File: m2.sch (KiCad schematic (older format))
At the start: 16 parts, among them M2 M2_2280, U12 MDT580M01001

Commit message: Cleanup
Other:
- note removed: "Work in progress."
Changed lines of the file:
@@
 $Descr A4 11693 8268
 encoding utf-8
-Sheet 8 13
+Sheet 8 12
 Title ""
 Date ""
@@
 	1    0    0    -1
 $EndComp
-Text Notes 2725 1200 0    50   ~ 0
-Work in progress.
 Text Notes 2669 49363 0    60   ~ 0
 Text

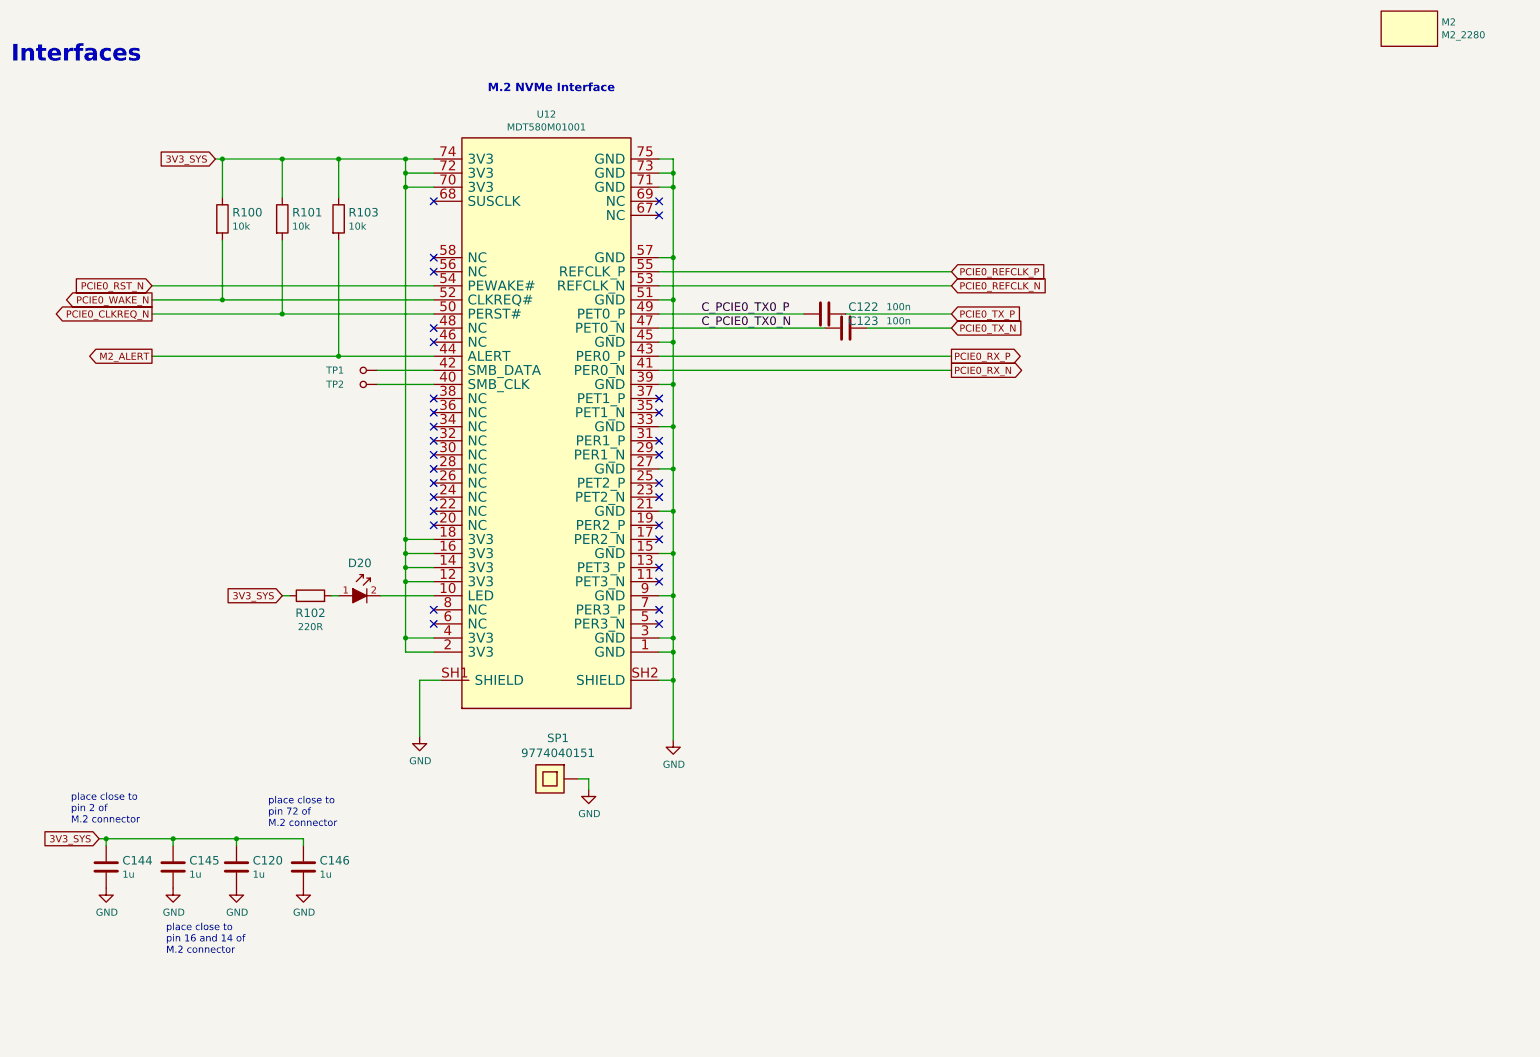
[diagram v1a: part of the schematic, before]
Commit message: Reorganize schematics, add descriptions in top left corner
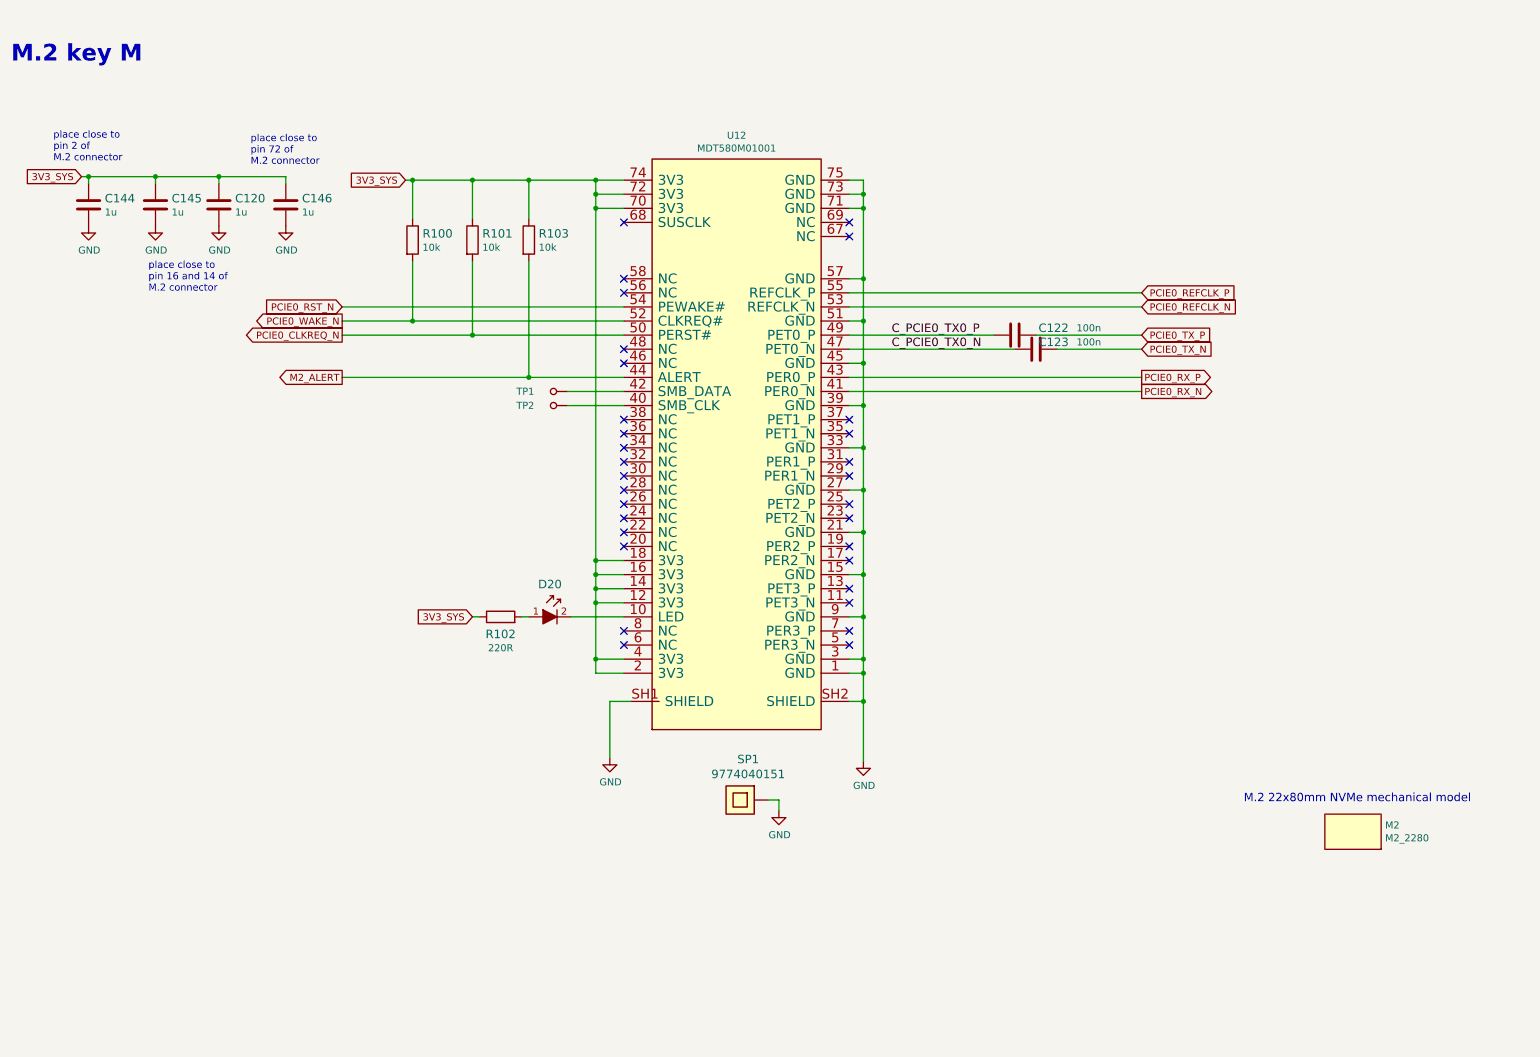
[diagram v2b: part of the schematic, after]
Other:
- note added: "M.2 22x80mm NVMe mechanical model"
- note added: "M.2 key M"
- note removed: "Interfaces"
- note removed: "M.2 NVMe Interface"
- moved on the sheet: C120, C122, C123, C144, C145, C146, D20, M2, R100, R101, R102, R103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

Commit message: Clear annotation and annotate
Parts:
- renumbered C144 to C111, C145 to C112, C120 to C113, C146 to C114, C122 to C115, C123 to C116, D20 to D21, R100 to R90, R101 to R91, R102 to R92, R103 to R93, SP1 to SP5, TP1 to TP42, TP2 to TP43, U12 to U15
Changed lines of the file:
@@
 $EndDescr
 $Comp
-L sa800u-baseboard-hw:MDT580M01001 U12
+L sa800u-baseboard-hw:MDT580M01001 U15
 U 1 1 61A7DEAD
 P 5825 3975
-F 0 "U12" H 5825 6542 50  0000 C CNN
+F 0 "U15" H 5825 6542 50  0000 C CNN
 F 1 "MDT580M01001" H 5825 6451 50  0000 C CNN
 F 2 "sa800u-baseboard-hw-footprints:MDT580M01001" H 5825 3975 50  0001 C CNN
@@
 NoConn ~ 5025 2025
 $Comp
-L sa800u-baseboard-hw:R_10k_0402 R100
+L sa800u-baseboard-hw:R_10k_0402 R90
 U 1 1 61EFBC15
 P 3525 2150
-F 0 "R100" V 3480 2220 60  0000 L CNN
+F 0 "R90" V 3480 2220 60  0000 L CNN
 F 1 "R_10k_0402" H 3525 2000 60  0001 C CNN
 F 2 "sa800u-baseboard-hw-footprints:0402-res" H 3725 2350 60  0001 L CNN
@@
 $EndComp
 $Comp
-L sa800u-baseboard-hw:R_10k_0402 R101
+L sa800u-baseboard-hw:R_10k_0402 R91
 U 1 1 61EFDAC5
 P 3950 2150
-F 0 "R101" V 3905 2220 60  0000 L CNN
+F 0 "R91" V 3905 2220 60  0000 L CNN
 F 1 "R_10k_0402" H 3950 2000 60  0001 C CNN
 F 2 "sa800u-baseboard-hw-footprints:0402-res" H 4150 2350 60  0001 L CNN
@@
 $EndComp
 $Comp
-L sa800u-baseboard-hw:R_10k_0402 R103
+L sa800u-baseboard-hw:R_10k_0402 R93
 U 1 1 61F0124E
 P 4350 2150
-F 0 "R103" V 4305 2220 60  0000 L CNN
+F 0 "R93" V 4305 2220 60  0000 L CNN
 F 1 "R_10k_0402" H 4350 2000 60  0001 C CNN
 F 2 "sa800u-baseboard-hw-footprints:0402-res" H 4550 2350 60  0001 L CNN
@@
 $EndComp
 $Comp
-L sa800u-baseboard-hw:R_220R_0402 R102
+L sa800u-baseboard-hw:R_220R_0402 R92
 U 1 1 61F0A68A
 P 4150 4825
-F 0 "R102" H 4150 4702 60  0000 C CNN
+F 0 "R92" H 4150 4702 60  0000 C CNN
 F 1 "R_220R_0402" H 4150 4675 60  0001 C CNN
 F 2 "sa800u-baseboard-hw-footprints:0402-res" H 4350 5025 60  0001 L CNN
@@
 $EndComp
 $Comp
-L sa800u-baseboard-hw:C_1u_0402 C120
+L sa800u-baseboard-hw:C_1u_0402 C113
 U 1 1 61F18D5F
 P 2150 1900
-F 0 "C120" H 2265 1945 60  0000 L CNN
+F 0 "C113" H 2265 1945 60  0000 L CNN
 F 1 "C_1u_0402" H 2150 1750 60  0001 C CNN
 F 2 "sa800u-baseboard-hw-footprints:0402-cap" H 2350 2100 60  0001 L CNN
@@
 P 2150 2050
 AR Path="/61B0DC30/61F20AE2" Ref="#PWR?"  Part="1"
-AR Path="/61B13669/61F20AE2" Ref="#PWR0179"  Part="1"
-F 0 "#PWR0179" H 2150 1800 50  0001 C CNN
+AR Path="/61B13669/61F20AE2" Ref="#PWR0184"  Part="1"
+F 0 "#PWR0184" H 2150 1800 50  0001 C CNN
 F 1 "GND" H 2155 1877 50  0000 C CNN
 F 2 "" H 2150 2050 50  0001 C CNN
@@
 $EndComp
 $Comp
-L sa800u-baseboard-hw:C_100n_0402 C122
+L sa800u-baseboard-hw:C_100n_0402 C115
 U 1 1 61F2C5C0
 P 7800 2825
-F 0 "C122" V 7850 2550 60  0000 C CNN
+F 0 "C115" V 7850 2550 60  0000 C CNN
 F 1 "C_100n_0402" H 7800 2675 60  0001 C CNN
 F 2 "sa800u-baseboard-hw-footprints:0402-cap" H 8000 3025 60  0001 L CNN
@@
 $EndComp
 $Comp
-L sa800u-baseboard-hw:C_100n_0402 C123
+L sa800u-baseboard-hw:C_100n_0402 C116
 U 1 1 61F30E44
 P 7950 2925
-F 0 "C123" V 8000 2800 60  0000 C CNN
+F 0 "C116" V 8000 2800 60  0000 C CNN
 F 1 "C_100n_0402" H 7950 2775 60  0001 C CNN
 F 2 "sa800u-baseboard-hw-footprints:0402-cap" H 8150 3125 60  0001 L CNN
@@
 $EndComp
 $Comp
-L sa800u-baseboard-hw:9774040151 SP1
+L sa800u-baseboard-hw:9774040151 SP5
 U 1 1 61F46DD9
 P 5850 6125
-F 0 "SP1" H 5793 5836 60  0000 C CNN
+F 0 "SP5" H 5793 5836 60  0000 C CNN
 F 1 "9774040151" H 5793 5942 60  0000 C CNN
 F 2 "sa800u-baseboard-hw-footprints:9774040151" H 5850 6125 60  0001 C CNN
@@
 P 6125 6200
 AR Path="/61B0DC30/61F4FB29" Ref="#PWR?"  Part="1"
-AR Path="/61B13669/61F4FB29" Ref="#PWR0181"  Part="1"
-F 0 "#PWR0181" H 6125 5950 50  0001 C CNN
+AR Path="/61B13669/61F4FB29" Ref="#PWR0187"  Part="1"
+F 0 "#PWR0187" H 6125 5950 50  0001 C CNN
 F 1 "GND" H 6130 6027 50  0000 C CNN
 F 2 "" H 6125 6200 50  0001 C CNN
@@
 P 6725 5850
 AR Path="/61B0DC30/61F53FFE" Ref="#PWR?"  Part="1"
-AR Path="/61B13669/61F53FFE" Ref="#PWR0182"  Part="1"
-F 0 "#PWR0182" H 6725 5600 50  0001 C CNN
+AR Path="/61B13669/61F53FFE" Ref="#PWR0188"  Part="1"
+F 0 "#PWR0188" H 6725 5600 50  0001 C CNN
 F 1 "GND" H 6730 5677 50  0000 C CNN
 F 2 "" H 6725 5850 50  0001 C CNN
@@
 P 4925 5825
 AR Path="/61B0DC30/61F57A1D" Ref="#PWR?"  Part="1"
-AR Path="/61B13669/61F57A1D" Ref="#PWR0183"  Part="1"
-F 0 "#PWR0183" H 4925 5575 50  0001 C CNN
+AR Path="/61B13669/61F57A1D" Ref="#PWR0186"  Part="1"
+F 0 "#PWR0186" H 4925 5575 50  0001 C CNN
 F 1 "GND" H 4930 5652 50  0000 C CNN
 F 2 "" H 4925 5825 50  0001 C CNN
@@
 	4350 1725 4825 1725
 $Comp
-L sa800u-baseboard-hw:TP_SMD_0_75MM TP1
+L sa800u-baseboard-hw:TP_SMD_0_75MM TP42
 U 1 1 61F6D551
 P 4525 3225
-F 0 "TP1" V 4525 3025 50  0000 C CNN
+F 0 "TP42" V 4525 3025 50  0000 C CNN
 F 1 "TP_SMD_0_75MM" H 4525 3125 50  0001 C CNN
 F 2 "sa800u-baseboard-hw-footprints:Testpoint_smd_0_75mm" H 4725 3425 60  0001 L CNN
@@
 $EndComp
 $Comp
-L sa800u-baseboard-hw:TP_SMD_0_75MM TP2
+L sa800u-baseboard-hw:TP_SMD_0_75MM TP43
 U 1 1 61F6FD56
 P 4525 3325
-F 0 "TP2" V 4525 3125 50  0000 C CNN
+F 0 "TP43" V 4525 3125 50  0000 C CNN
 F 1 "TP_SMD_0_75MM" H 4525 3225 50  0001 C CNN
 F 2 "sa800u-baseboard-hw-footprints:Testpoint_smd_0_75mm" H 4725 3525 60  0001 L CNN
@@
 	1700 1700 1700 1750
 $Comp
-L sa800u-baseboard-hw:C_1u_0402 C145
+L sa800u-baseboard-hw:C_1u_0402 C112
 U 1 1 62813726
 P 1700 1900
-F 0 "C145" H 1815 1945 60  0000 L CNN
+F 0 "C112" H 1815 1945 60  0000 L CNN
 F 1 "C_1u_0402" H 1700 1750 60  0001 C CNN
 F 2 "sa800u-baseboard-hw-footprints:0402-cap" H 1900 2100 60  0001 L CNN
@@
 P 1700 2050
 AR Path="/61B0DC30/6281372C" Ref="#PWR?"  Part="1"
-AR Path="/61B13669/6281372C" Ref="#PWR0175"  Part="1"
-F 0 "#PWR0175" H 1700 1800 50  0001 C CNN
+AR Path="/61B13669/6281372C" Ref="#PWR0183"  Part="1"
+F 0 "#PWR0183" H 1700 1800 50  0001 C CNN
 F 1 "GND" H 1705 1877 50  0000 C CNN
 F 2 "" H 1700 2050 50  0001 C CNN
@@
 	1225 1700 1225 1750
 $Comp
-L sa800u-baseboard-hw:C_1u_0402 C144
+L sa800u-baseboard-hw:C_1u_0402 C111
 U 1 1 6281A9A2
 P 1225 1900
-F 0 "C144" H 1340 1945 60  0000 L CNN
+F 0 "C111" H 1340 1945 60  0000 L CNN
 F 1 "C_1u_0402" H 1225 1750 60  0001 C CNN
 F 2 "sa800u-baseboard-hw-footprints:0402-cap" H 1425 2100 60  0001 L CNN
@@
 P 1225 2050
 AR Path="/61B0DC30/6281A9A8" Ref="#PWR?"  Part="1"
-AR Path="/61B13669/6281A9A8" Ref="#PWR0176"  Part="1"
-F 0 "#PWR0176" H 1225 1800 50  0001 C CNN
+AR Path="/61B13669/6281A9A8" Ref="#PWR0182"  Part="1"
+F 0 "#PWR0182" H 1225 1800 50  0001 C CNN
 F 1 "GND" H 1230 1877 50  0000 C CNN
 F 2 "" H 1225 2050 50  0001 C CNN
@@
 	2625 1700 2625 1750
 $Comp
-L sa800u-baseboard-hw:C_1u_0402 C146
+L sa800u-baseboard-hw:C_1u_0402 C114
 U 1 1 6282B4A7
 P 2625 1900
-F 0 "C146" H 2740 1945 60  0000 L CNN
+F 0 "C114" H 2740 1945 60  0000 L CNN
 F 1 "C_1u_0402" H 2625 1750 60  0001 C CNN
 F 2 "sa800u-baseboard-hw-footprints:0402-cap" H 2825 2100 60  0001 L CNN
@@
 P 2625 2050
 AR Path="/61B0DC30/6282B4AD" Ref="#PWR?"  Part="1"
-AR Path="/61B13669/6282B4AD" Ref="#PWR0177"  Part="1"
-F 0 "#PWR0177" H 2625 1800 50  0001 C CNN
+AR Path="/61B13669/6282B4AD" Ref="#PWR0185"  Part="1"
+F 0 "#PWR0185" H 2625 1800 50  0001 C CNN
 F 1 "GND" H 2630 1877 50  0000 C CNN
 F 2 "" H 2625 2050 50  0001 C CNN
@@
 P 4550 4825
 AR Path="/61B0DC30/621C05D4" Ref="D?"  Part="1"
-AR Path="/61B13669/621C05D4" Ref="D20"  Part="1"
-F 0 "D20" H 4500 5056 60  0000 C CNN
+AR Path="/61B13669/621C05D4" Ref="D21"  Part="1"
+F 0 "D21" H 4500 5056 60  0000 C CNN
 F 1 "KP-1608EC" H 4500 5056 60  0001 C CNN
 F 2 "sa800u-baseboard-hw-footprints:LED_0603" H 4750 5025 60  0001 L CNN
